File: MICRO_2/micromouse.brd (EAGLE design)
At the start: 100 x 80 mm, 27 parts

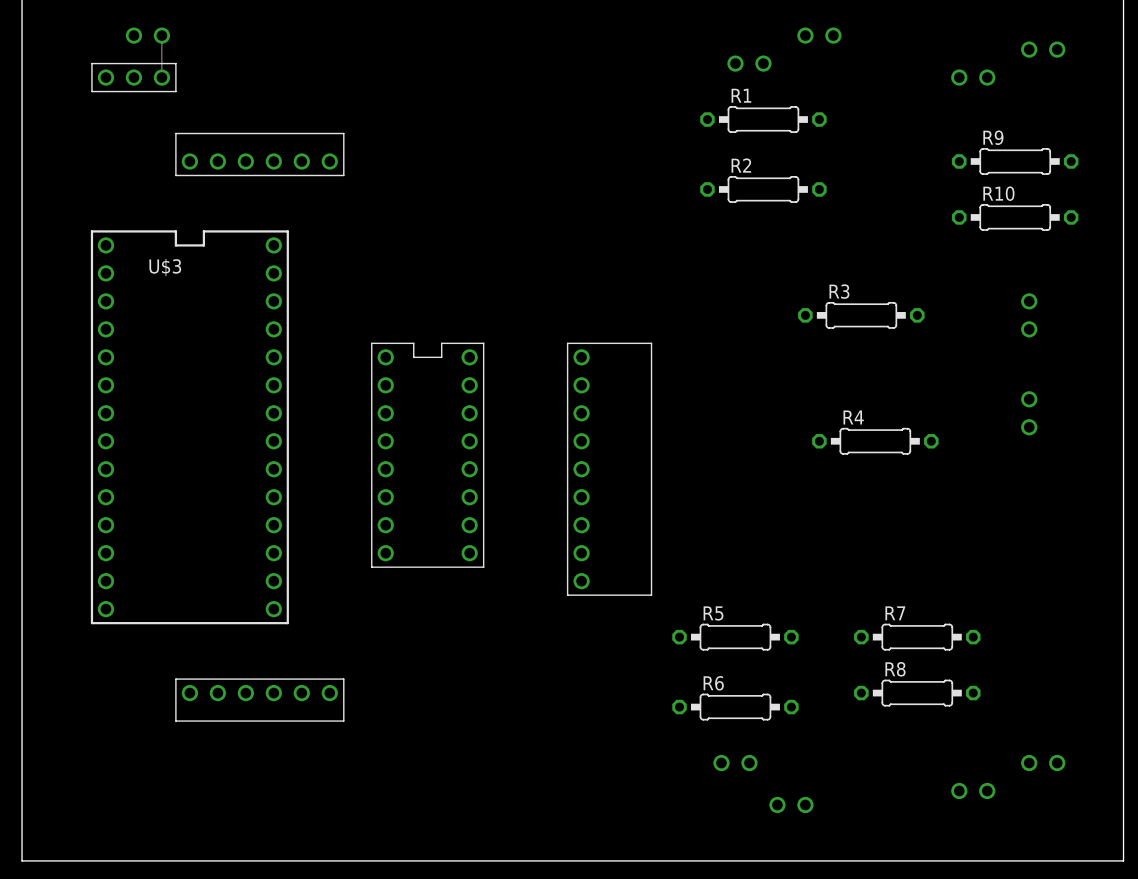
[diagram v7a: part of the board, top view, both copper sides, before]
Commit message: put in more traces
fall back to this if putting all traces on a single layer does not work
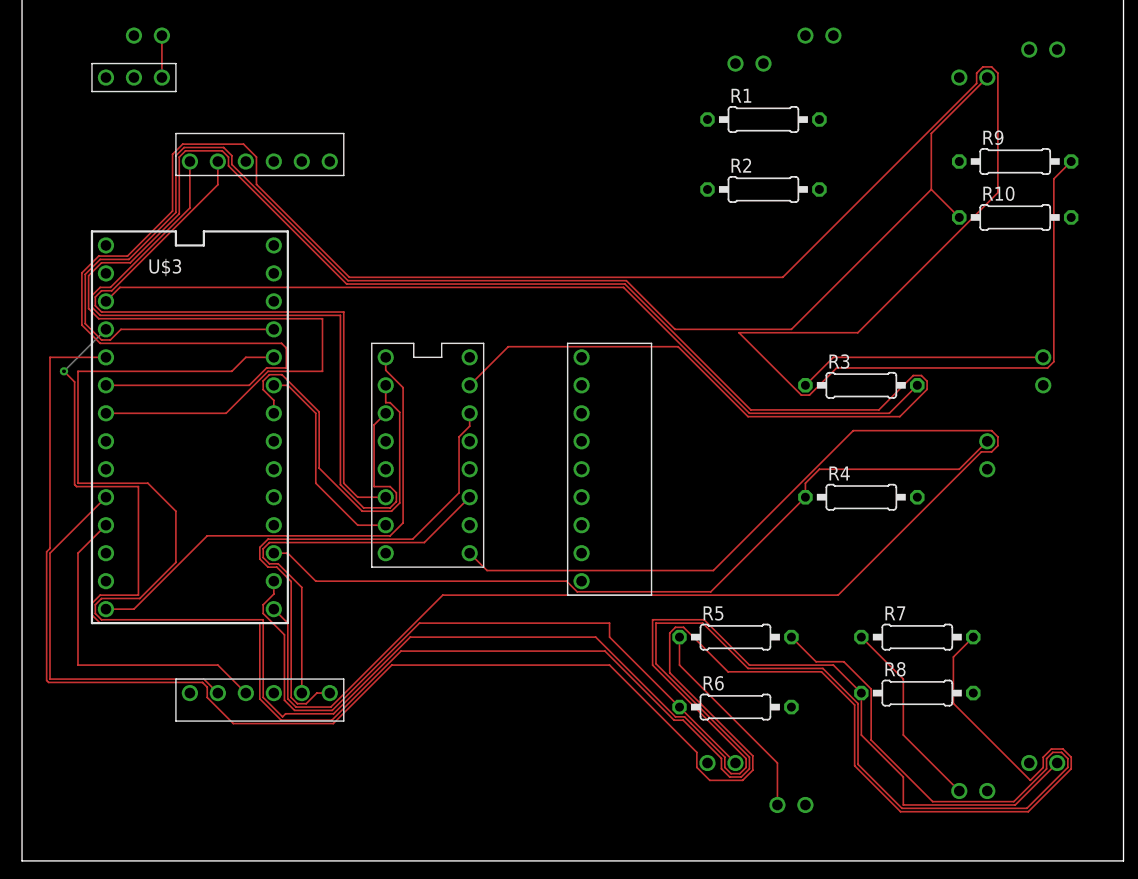
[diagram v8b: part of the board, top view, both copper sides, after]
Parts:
- moved R3 6.35 mm to (76.2, 43.2)
- moved U$12 5.39 mm to (87.6, 36.8)
- moved R4 5.24 mm to (76.2, 33.0)
- moved U$6 5.24 mm to (92.7, 45.7)
- moved U$8 1.27 mm to (63.5, 8.89)
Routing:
- net N$9: track 0.00 -> 239.8 mm
- net N$25: track 0.00 -> 216.5 mm, vias 0 -> 1
- net N$6: track 0.00 -> 196.0 mm
- net N$8: track 0.00 -> 194.7 mm
- net N$5: track 0.00 -> 193.5 mm
- net M2_ENABLE: track 0.00 -> 138.2 mm
- net N$12: track 0.00 -> 135.6 mm
- net N$22: track 0.00 -> 80.0 mm
- net N$24: track 0.00 -> 72.6 mm
- net M1_L: track 0.00 -> 72.0 mm
- net N$21: track 0.00 -> 62.6 mm
- net M2_L: track 0.00 -> 60.9 mm
- net M1_R: track 0.00 -> 47.2 mm
- net N$4: track 0.00 -> 45.9 mm
- net M1_FWD_PWM: track 0.00 -> 35.8 mm
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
